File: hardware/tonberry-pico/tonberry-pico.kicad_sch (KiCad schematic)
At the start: 28 parts, among them J1 MicroSD_Breakout, J2 SparkFun I2S Audio Breakout M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, J3 RC522_Breakout, J4 Adafruit_bq25185_5V, J5 UART, J6 WS2812, J7 Buttons, Q1 2N7000, Q2 2N7000, SW1 SW_Push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

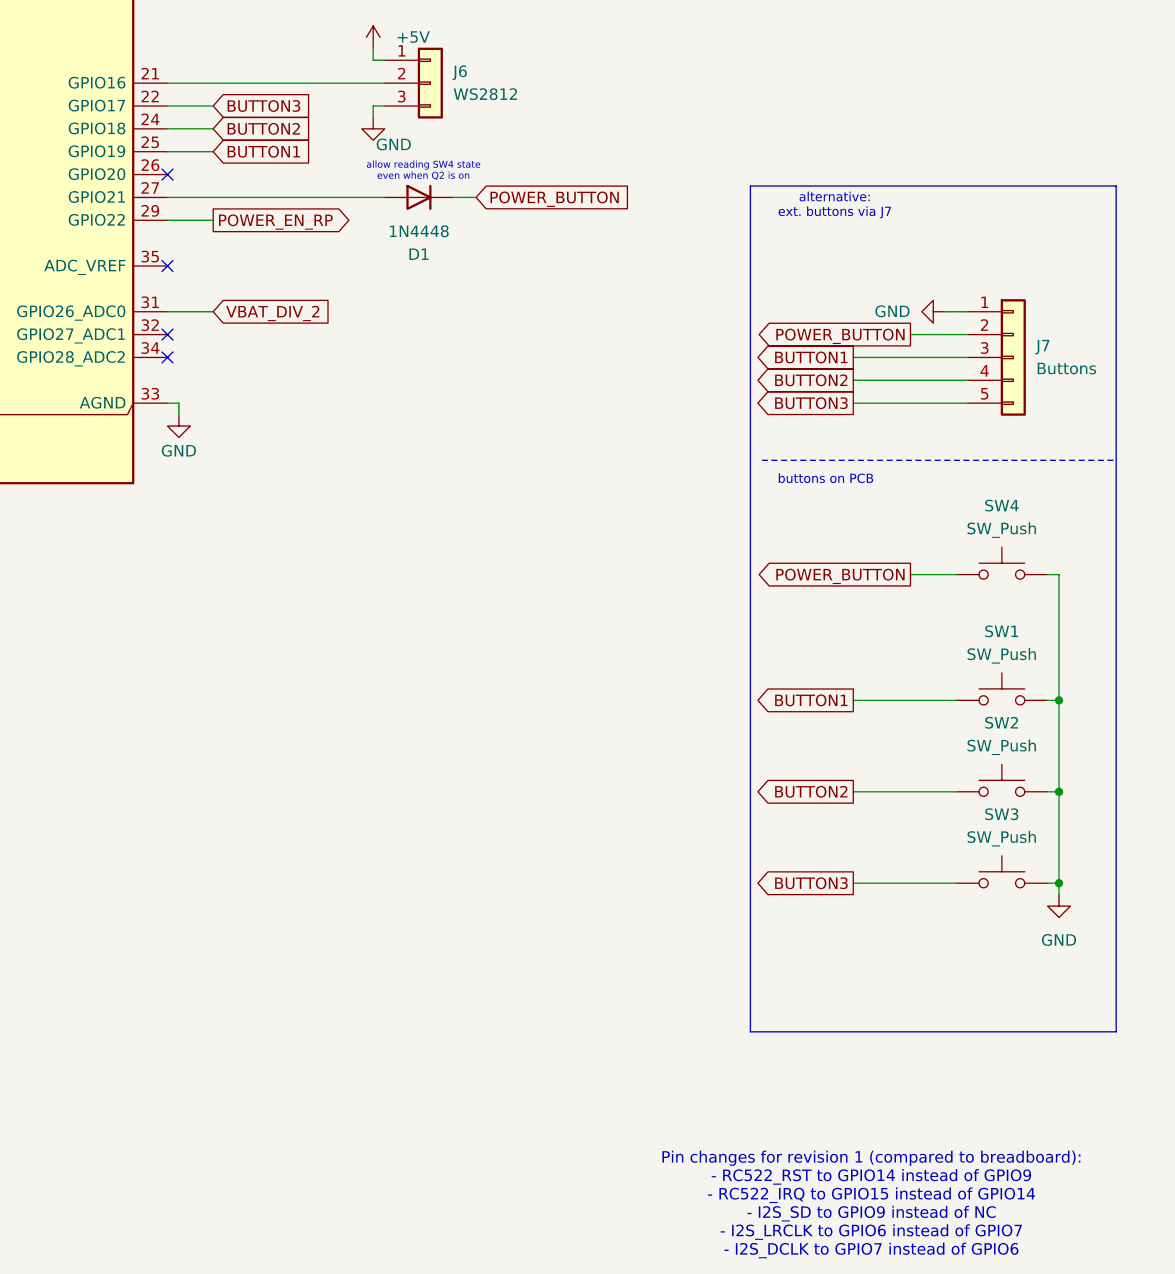
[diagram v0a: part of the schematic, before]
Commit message: hw: Add fifth button, make traces wider
Signed-off-by: Matthias Blankertz <matthias@blankertz.org>
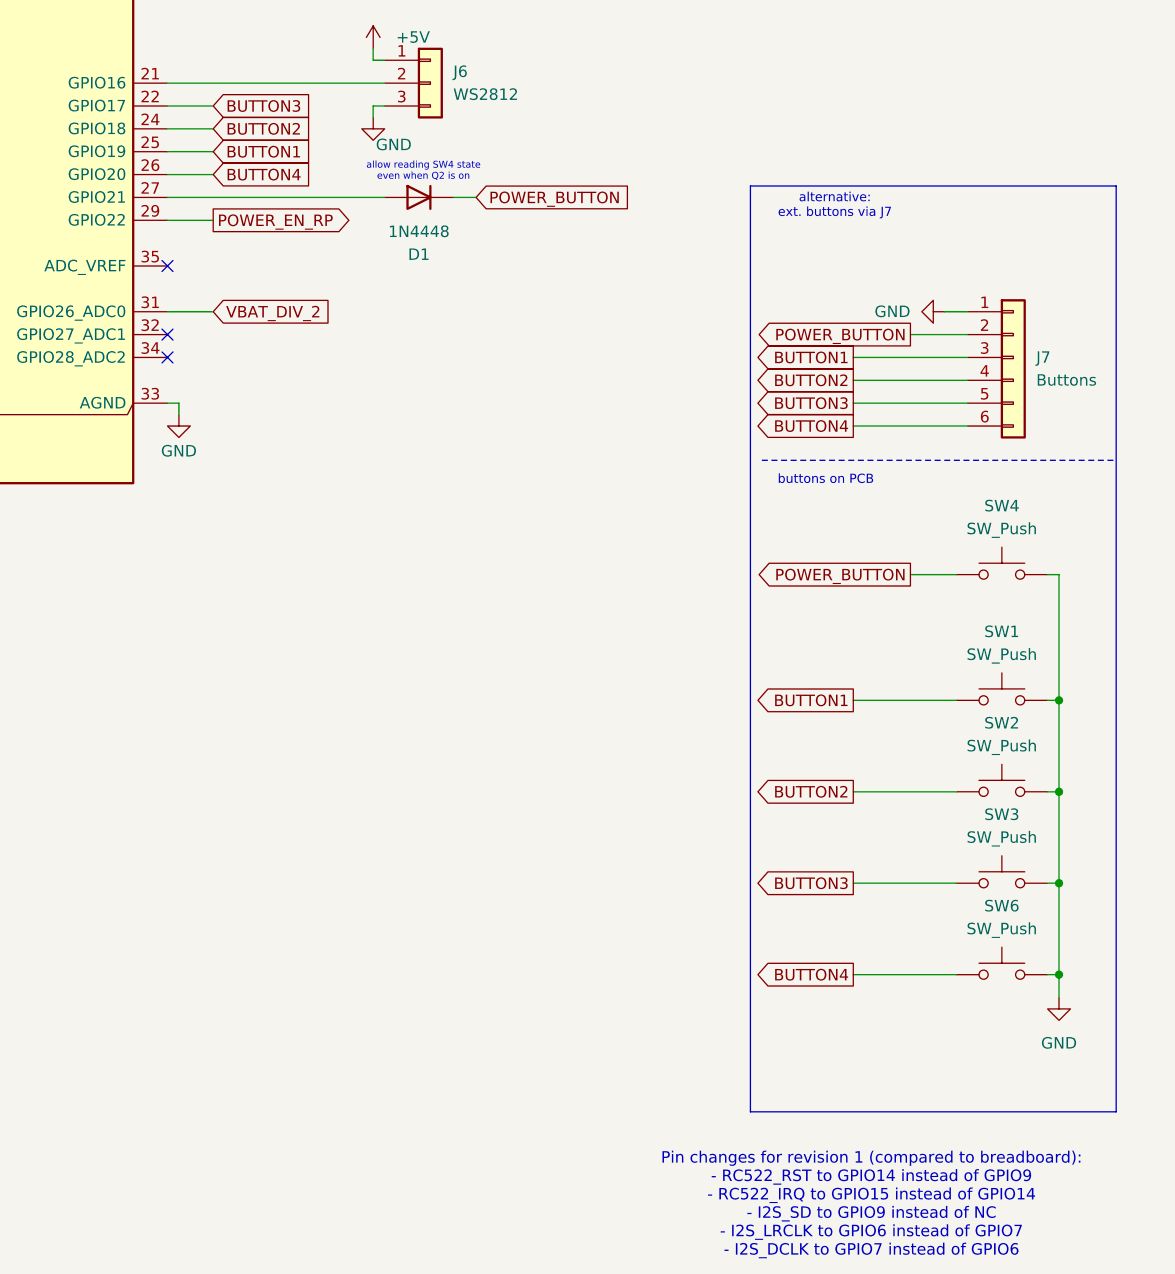
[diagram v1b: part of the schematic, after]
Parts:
- added SW6: SW_Push, Button_Switch_THT:Push_E-Switch_KS01Q01, symbol Switch:SW_Push
- J6: footprint Connector_PinSocket_2.54mm:PinSocket_1x03_P2.54mm_Vertical -> Connector_PinHeader_2.54mm:PinHeader_1x03_P2.54mm_Vertical
- J7: footprint Connector_PinSocket_2.54mm:PinSocket_1x05_P2.54mm_Vertical -> Connector_PinHeader_2.54mm:PinHeader_1x06_P2.54mm_Vertical; symbol Connector_Generic:Conn_01x05 -> Connector_Generic:Conn_01x06
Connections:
- net GND: now also SW6.2
- net BUTTON4: now reaches U1.26 (GPIO20)
- net BUTTON4: now also J7.6 (Pin_6), SW6.1
- no-connect marks 9 -> 8
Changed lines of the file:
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@@
 	(rectangle
 		(start 242.57 60.96)
-		(end 283.21 154.94)
+		(end 283.21 163.83)
 		(stroke
 			(width 0)
@@
 	)
 	(junction
+		(at 276.86 148.59)
+		(diameter 0)
+		(color 0 0 0 0)
+	)
+	(junction
 		(at 55.88 45.72)
 		(diameter 0)
@@
 	)
 	(no_connect
-		(at 177.8 59.69)
-	)
-	(no_connect
 		(at 177.8 69.85)
 	)
@@
 	(wire
 		(pts
+			(xy 276.86 148.59) (xy 276.86 151.13)
+		)
+		(stroke
+			(width 0)
+			(type default)
+		)
+	)
+	(wire
+		(pts
 			(xy 254 138.43) (xy 265.43 138.43)
 		)
@@
 	(wire
 		(pts
+			(xy 275.59 148.59) (xy 276.86 148.59)
+		)
+		(stroke
+			(width 0)
+			(type default)
+		)
+	)
+	(wire
+		(pts
 			(xy 276.86 128.27) (xy 276.86 138.43)
 		)
@@
 	(wire
 		(pts
+			(xy 254 87.63) (xy 266.7 87.63)
+		)
+		(stroke
+			(width 0)
+			(type default)
+		)
+	)
+	(wire
+		(pts
 			(xy 85.09 170.18) (xy 72.39 170.18)
 		)
@@
 	(wire
 		(pts
-			(xy 276.86 138.43) (xy 276.86 139.7)
+			(xy 276.86 138.43) (xy 276.86 148.59)
 		)
 		(stroke
@@
 	(wire
 		(pts
+			(xy 177.8 59.69) (xy 182.88 59.69)
+		)
+		(stroke
+			(width 0)
+			(type default)
+		)
+	)
+	(wire
+		(pts
 			(xy 49.53 162.56) (xy 49.53 190.5)
 		)
@@
 	(wire
 		(pts
+			(xy 254 148.59) (xy 265.43 148.59)
+		)
+		(stroke
+			(width 0)
+			(type default)
+		)
+	)
+	(wire
+		(pts
 			(xy 52.07 55.88) (xy 52.07 69.85)
 		)
@@
 		)
 	)
+	(global_label "BUTTON4"
+		(shape output)
+		(at 254 87.63 180)
+		(fields_autoplaced yes)
+		(effects
+			(font
+				(size 1.27 1.27)
+			)
+			(justify right)
+		)
+		(property "Intersheetrefs" "${INTERSHEET_REFS}"
+			(at 242.6086 87.63 0)
+			(effects
+				(font
+					(size 1.27 1.27)
+				)
+				(justify right)
+				(hide yes)
+			)
+		)
+	)
 	(global_label "BUTTON1"
 		(shape output)
@@
 		)
 	)
+	(global_label "BUTTON4"
+		(shape input)
+		(at 182.88 59.69 0)
+		(fields_autoplaced yes)
+		(effects
+			(font
+				(size 1.27 1.27)
+			)
+			(justify left)
+		)
+		(property "Intersheetrefs" "${INTERSHEET_REFS}"
+			(at 194.2714 59.69 0)
+			(effects
+				(font
+					(size 1.27 1.27)
+				)
+				(justify left)
+				(hide yes)
+			)
+		)
+	)
 	(global_label "BUTTON2"
 		(shape output)
@@
 		)
 	)
+	(global_label "BUTTON4"
+		(shape output)
+		(at 254 148.59 180)
+		(fields_autoplaced yes)
+		(effects
+			(font
+				(size 1.27 1.27)
+			)
+			(justify right)
+		)
+		(property "Intersheetrefs" "${INTERSHEET_REFS}"
+			(at 242.6086 148.59 0)
+			(effects
+				(font
+					(size 1.27 1.27)
+				)
+				(justify right)
+				(hide yes)
+			)
+		)
+	)
 	(global_label "POWER_BUTTON"
 		(shape input)
@@
 			)
 		)
-		(property "Footprint" "Connector_PinSocket_2.54mm:PinSocket_1x03_P2.54mm_Vertical"
+		(property "Footprint" "Connector_PinHeader_2.54mm:PinHeader_1x03_P2.54mm_Vertical"
 			(at 207.01 49.53 0)
 			(effects
@@
 	(symbol
 		(lib_id "power:GND")
-		(at 276.86 139.7 0)
+		(at 276.86 151.13 0)
 		(unit 1)
 		(exclude_from_sim no)
@@
 		(fields_autoplaced yes)
 		(property "Reference" "#PWR013"
-			(at 276.86 146.05 0)
+			(at 276.86 157.48 0)
 			(effects
 				(font
@@
 		)
 		(property "Value" "GND"
-			(at 276.86 144.78 0)
+			(at 276.86 156.21 0)
 			(effects
 				(font
@@
 		)
 		(property "Footprint" ""
-			(at 276.86 139.7 0)
+			(at 276.86 151.13 0)
 			(effects
 				(font
@@
 		)
 		(property "Datasheet" ""
-			(at 276.86 139.7 0)
+			(at 276.86 151.13 0)
 			(effects
 				(font
@@
 		)
 		(property "Description" "Power symbol creates a global label with name \"GND\" , ground"
-			(at 276.86 139.7 0)
+			(at 276.86 151.13 0)
 			(effects
 				(font
@@
 	)
 	(symbol
+		(lib_id "Switch:SW_Push")
+		(at 270.51 148.59 0)
+		(unit 1)
+		(exclude_from_sim no)
+		(in_bom yes)
+		(on_board yes)
+		(dnp no)
+		(fields_autoplaced yes)
+		(property "Reference" "SW6"
+			(at 270.51 140.97 0)
+			(effects
+				(font
+					(size 1.27 1.27)
+				)
+			)
+		)
+		(property "Value" "SW_Push"
+			(at 270.51 143.51 0)
+			(effects
+				(font
+					(size 1.27 1.27)
+				)
+			)
+		)
+		(property "Footprint" "Button_Switch_THT:Push_E-Switch_KS01Q01"
+			(at 270.51 143.51 0)
+			(effects
+				(font
+					(size 1.27 1.27)
+				)
+				(hide yes)
+			)
+		)
+		(property "Datasheet" "~"
+			(at 270.51 143.51 0)
+			(effects
+				(font
+					(size 1.27 1.27)
+				)
+				(hide yes)
+			)
+		)
+		(property "Description" "Push button switch, generic, two pins"
+			(at 270.51 148.59 0)
+			(effects
+				(font
+					(size 1.27 1.27)
+				)
+				(hide yes)
+			)
+		)
+		(pin "1"
+		)
+		(pin "2"
+		)
+		(instances
+			(project "tonberry-pico"
+				(path "/7226ca0f-138a-46b4-89f3-dc32dfb1f9f7"
+					(reference "SW6")
+					(unit 1)
+				)
+			)
+		)
+	)
+	(symbol
 		(lib_id "Connector_Generic:Conn_01x03")
 		(at 115.57 31.75 90)
@@
 	)
 	(symbol
-		(lib_id "Connector_Generic:Conn_01x05")
+		(lib_id "Connector_Generic:Conn_01x06")
 		(at 271.78 80.01 0)
 		(unit 1)
@@
 		(fields_autoplaced yes)
 		(property "Reference" "J7"
-			(at 274.32 78.7399 0)
+			(at 274.32 80.0099 0)
 			(effects
 				(font
@@
 		)
 		(property "Value" "Buttons"
-			(at 274.32 81.2799 0)
+			(at 274.32 82.5499 0)
 			(effects
 				(font
@@
 			)
 		)
-		(property "Footprint" "Connector_PinSocket_2.54mm:PinSocket_1x05_P2.54mm_Vertical"
+		(property "Footprint" "Connector_PinHeader_2.54mm:PinHeader_1x06_P2.54mm_Vertical"
 			(at 271.78 80.01 0)
 			(effects
@@
 			)
 		)
-		(property "Description" "Generic connector, single row, 01x05, script generated (kicad-library-utils/schlib/autogen/connector/)"
+		(property "Description" "Generic connector, single row, 01x06, script generated (kicad-library-utils/schlib/autogen/connector/)"
 			(at 271.78 80.01 0)
 			(effects
@@
 		(pin "1"
 		)
+		(pin "6"
+		)
 		(instances

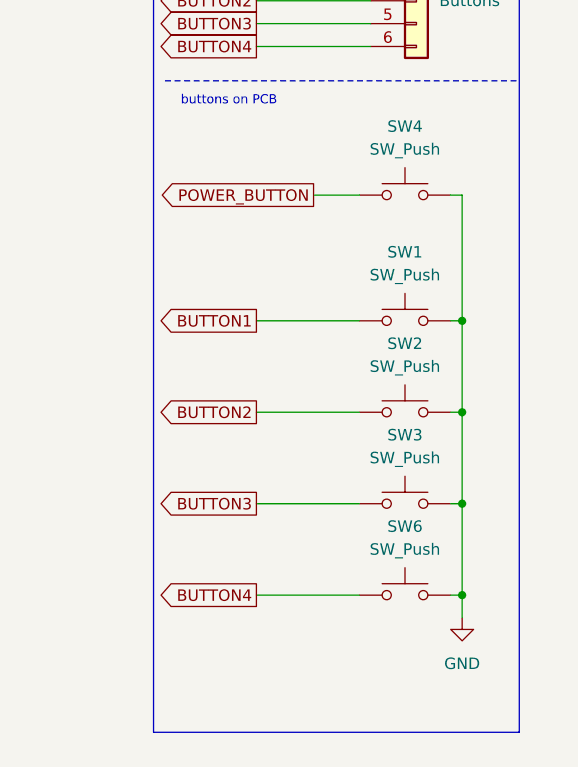
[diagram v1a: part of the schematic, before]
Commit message: hw: Smaller 'production' version of board w/o keys and direct RC522 mount
Signed-off-by: Matthias Blankertz <matthias@blankertz.org>
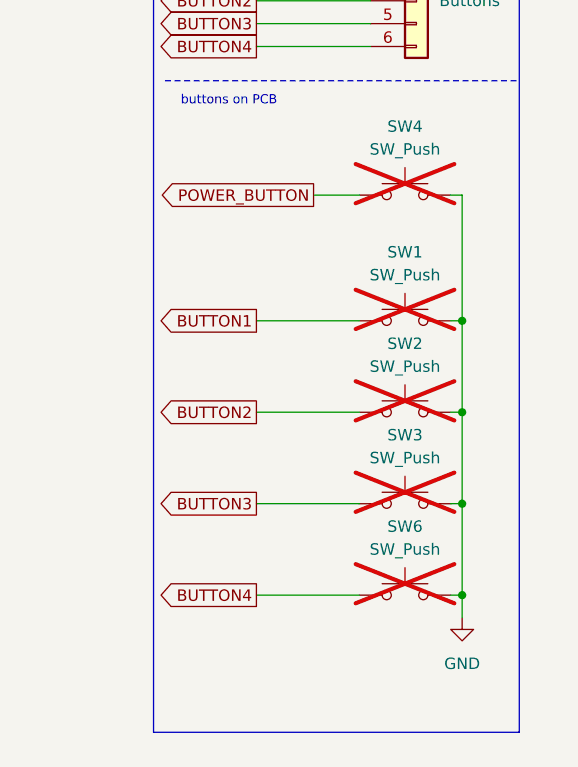
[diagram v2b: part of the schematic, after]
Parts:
- J3: footprint Modules:AZ_Delivery_RC522 -> Connector_PinSocket_2.54mm:PinSocket_1x08_P2.54mm_Vertical
- J6: footprint Connector_PinHeader_2.54mm:PinHeader_1x03_P2.54mm_Vertical -> Connector_JST:JST_XH_B3B-XH-A_1x03_P2.50mm_Vertical
- J7: footprint Connector_PinHeader_2.54mm:PinHeader_1x06_P2.54mm_Vertical -> Connector_JST:JST_XH_B6B-XH-A_1x06_P2.50mm_Vertical
- Q1, Q2: footprint Package_TO_SOT_THT:TO-92_Inline -> Package_TO_SOT_THT:TO-92_Inline_Wide
- SW1, SW2, SW3, SW4, SW6: now not fitted
- SW5: footprint Connector_PinHeader_2.54mm:PinHeader_1x02_P2.54mm_Vertical -> PCM_JLCPCB:SW_TS-1088-AR02016
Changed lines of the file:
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@@
 			)
 		)
-		(property "Footprint" "Connector_PinHeader_2.54mm:PinHeader_1x03_P2.54mm_Vertical"
+		(property "Footprint" "Connector_JST:JST_XH_B3B-XH-A_1x03_P2.50mm_Vertical"
 			(at 207.01 49.53 0)
 			(effects
@@
 			)
 		)
-		(property "Footprint" "Package_TO_SOT_THT:TO-92_Inline"
+		(property "Footprint" "Package_TO_SOT_THT:TO-92_Inline_Wide"
 			(at 58.42 172.085 0)
 			(effects
@@
 		(exclude_from_sim no)
 		(in_bom yes)
-		(on_board yes)
-		(dnp no)
+		(on_board no)
+		(dnp yes)
 		(fields_autoplaced yes)
 		(property "Reference" "SW3"
@@
 		(exclude_from_sim no)
 		(in_bom yes)
-		(on_board yes)
-		(dnp no)
+		(on_board no)
+		(dnp yes)
 		(property "Reference" "SW4"
 			(at 270.51 96.52 0)
@@
 			)
 		)
-		(property "Footprint" "Connector_PinHeader_2.54mm:PinHeader_1x02_P2.54mm_Vertical"
+		(property "Footprint" "PCM_JLCPCB:SW_TS-1088-AR02016"
 			(at 266.7 20.32 0)
 			(effects
@@
 		(exclude_from_sim no)
 		(in_bom yes)
-		(on_board yes)
-		(dnp no)
+		(on_board no)
+		(dnp yes)
 		(property "Reference" "SW1"
 			(at 270.51 110.49 0)
@@
 		(exclude_from_sim no)
 		(in_bom yes)
-		(on_board yes)
-		(dnp no)
+		(on_board no)
+		(dnp yes)
 		(fields_autoplaced yes)
 		(property "Reference" "SW2"
@@
 			)
 		)
-		(property "Footprint" "Modules:AZ_Delivery_RC522"
+		(property "Footprint" "Connector_PinSocket_2.54mm:PinSocket_1x08_P2.54mm_Vertical"
 			(at 74.93 90.17 0)
 			(effects
@@
 			)
 		)
-		(property "Footprint" "Package_TO_SOT_THT:TO-92_Inline"
+		(property "Footprint" "Package_TO_SOT_THT:TO-92_Inline_Wide"
 			(at 46.99 159.385 0)
 			(effects
@@
 		(exclude_from_sim no)
 		(in_bom yes)
-		(on_board yes)
-		(dnp no)
+		(on_board no)
+		(dnp yes)
 		(fields_autoplaced yes)
 		(property "Reference" "SW6"
@@
 			)
 		)
-		(property "Footprint" "Connector_PinHeader_2.54mm:PinHeader_1x06_P2.54mm_Vertical"
+		(property "Footprint" "Connector_JST:JST_XH_B6B-XH-A_1x06_P2.50mm_Vertical"
 			(at 271.78 80.01 0)
 			(effects

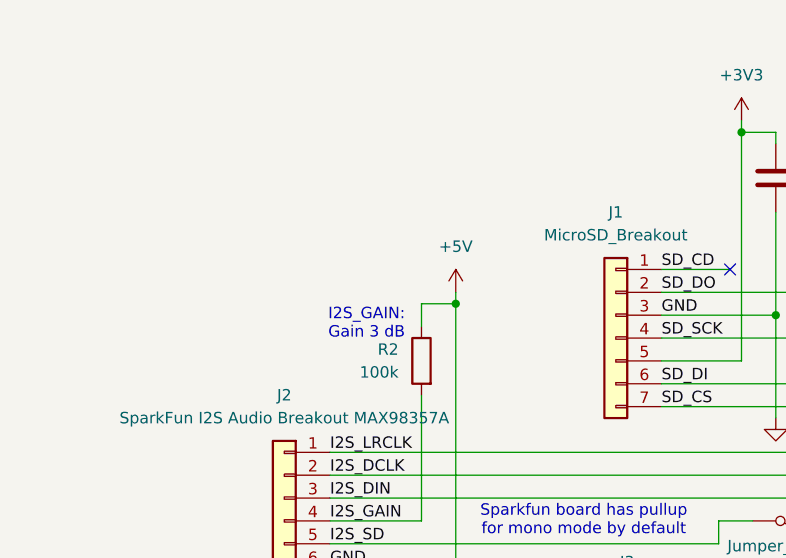
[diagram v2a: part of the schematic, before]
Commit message: hw: Add GND point for MAX98357 gain config
Add a through-hole pad connected to GND next to the MAX98357 gain config
resistor to allow the user to select from all possible gains.

Signed-off-by: Matthias Blankertz <matthias@blankertz.org>
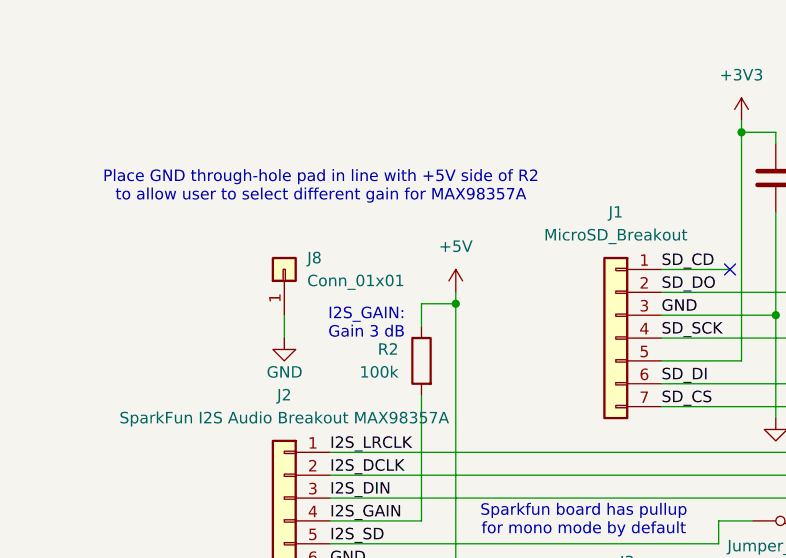
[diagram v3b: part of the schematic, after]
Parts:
- added J8: Conn_01x01, Connector_Wire:SolderWire-0.25sqmm_1x01_D0.65mm_OD1.7mm, symbol Connector_Generic:Conn_01x01
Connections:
- net GND: now also J8.1 (Pin_1)
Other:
- note added: "Place GND through-hole pad in line with +5V side of R2 to allow user to select different gain for MAX98357A"
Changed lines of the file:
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@@
 		)
 	)
+	(text "Place GND through-hole pad in line with +5V side of R2\nto allow user to select different gain for MAX98357A"
+		(exclude_from_sim no)
+		(at 40.894 32.766 0)
+		(effects
+			(font
+				(size 1.27 1.27)
+			)
+		)
+	)
 	(text "Battery power"
 		(exclude_from_sim no)
@@
 	(wire
 		(pts
+			(xy 36.83 46.99) (xy 36.83 49.53)
+		)
+		(stroke
+			(width 0)
+			(type default)
+		)
+	)
+	(wire
+		(pts
 			(xy 55.88 45.72) (xy 55.88 44.45)
 		)
@@
 	)
 	(symbol
+		(lib_id "power:GND")
+		(at 36.83 49.53 0)
+		(unit 1)
+		(exclude_from_sim no)
+		(in_bom yes)
+		(on_board yes)
+		(dnp no)
+		(property "Reference" "#PWR018"
+			(at 36.83 55.88 0)
+			(effects
+				(font
+					(size 1.27 1.27)
+				)
+				(hide yes)
+			)
+		)
+		(property "Value" "GND"
+			(at 38.862 53.34 0)
+			(effects
+				(font
+					(size 1.27 1.27)
+				)
+				(justify right)
+			)
+		)
+		(property "Footprint" ""
+			(at 36.83 49.53 0)
+			(effects
+				(font
+					(size 1.27 1.27)
+				)
+				(hide yes)
+			)
+		)
+		(property "Datasheet" ""
+			(at 36.83 49.53 0)
+			(effects
+				(font
+					(size 1.27 1.27)
+				)
+				(hide yes)
+			)
+		)
+		(property "Description" "Power symbol creates a global label with name \"GND\" , ground"
+			(at 36.83 49.53 0)
+			(effects
+				(font
+					(size 1.27 1.27)
+				)
+				(hide yes)
+			)
+		)
+		(pin "1"
+		)
+		(instances
+			(project "tonberry-pico"
+				(path "/7226ca0f-138a-46b4-89f3-dc32dfb1f9f7"
+					(reference "#PWR018")
+					(unit 1)
+				)
+			)
+		)
+	)
+	(symbol
 		(lib_id "Jumper:Jumper_2_Bridged")
 		(at 93.98 69.85 0)
@@
 					(unit 1)
 				)
+			)
+		)
+	)
+	(symbol
+		(lib_id "Connector_Generic:Conn_01x01")
+		(at 36.83 41.91 90)
+		(unit 1)
+		(exclude_from_sim no)
+		(in_bom yes)
+		(on_board yes)
+		(dnp no)
+		(fields_autoplaced yes)
+		(property "Reference" "J8"
+			(at 39.37 40.6399 90)
+			(effects
+				(font
+					(size 1.27 1.27)
+				)
+				(justify right)
+			)
+		)
+		(property "Value" "Conn_01x01"
+			(at 39.37 43.1799 90)
+			(effects
+				(font
+					(size 1.27 1.27)
+				)
+				(justify right)
+			)
+		)
+		(property "Footprint" "Connector_Wire:SolderWire-0.25sqmm_1x01_D0.65mm_OD1.7mm"
+			(at 36.83 41.91 0)
+			(effects
+				(font
+					(size 1.27 1.27)
+				)
+				(hide yes)
+			)
+		)
+		(property "Datasheet" "~"
+			(at 36.83 41.91 0)
+			(effects
+				(font
+					(size 1.27 1.27)
+				)
+				(hide yes)
+			)
+		)
+		(property "Description" "Generic connector, single row, 01x01, script generated (kicad-library-utils/schlib/autogen/connector/)"
+			(at 36.83 41.91 0)
+			(effects
+				(font
+					(size 1.27 1.27)
+				)
+				(hide yes)
+			)
+		)
+		(pin "1"
+		)
+		(instances
+			(project ""
+				(path "/7226ca0f-138a-46b4-89f3-dc32dfb1f9f7"
+					(reference "J8")
+					(unit 1)
+				)
